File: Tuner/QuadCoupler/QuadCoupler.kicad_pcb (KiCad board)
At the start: 2 copper layers, 100 x 100 mm, 78 parts, among them J1 Conn_01x02, J10 Conn_01x02, J2 Conn_Coaxial, J21 Conn_01x01, J22 Conn_01x01, J23 Conn_01x01, J24 Conn_01x01, J3 Conn_Coaxial, J4 Conn_Coaxial, J5 Conn_Coaxial, J6 Conn_Coaxial, J7 Conn_01x02, J8 Conn_01x02, J9 Conn_01x02

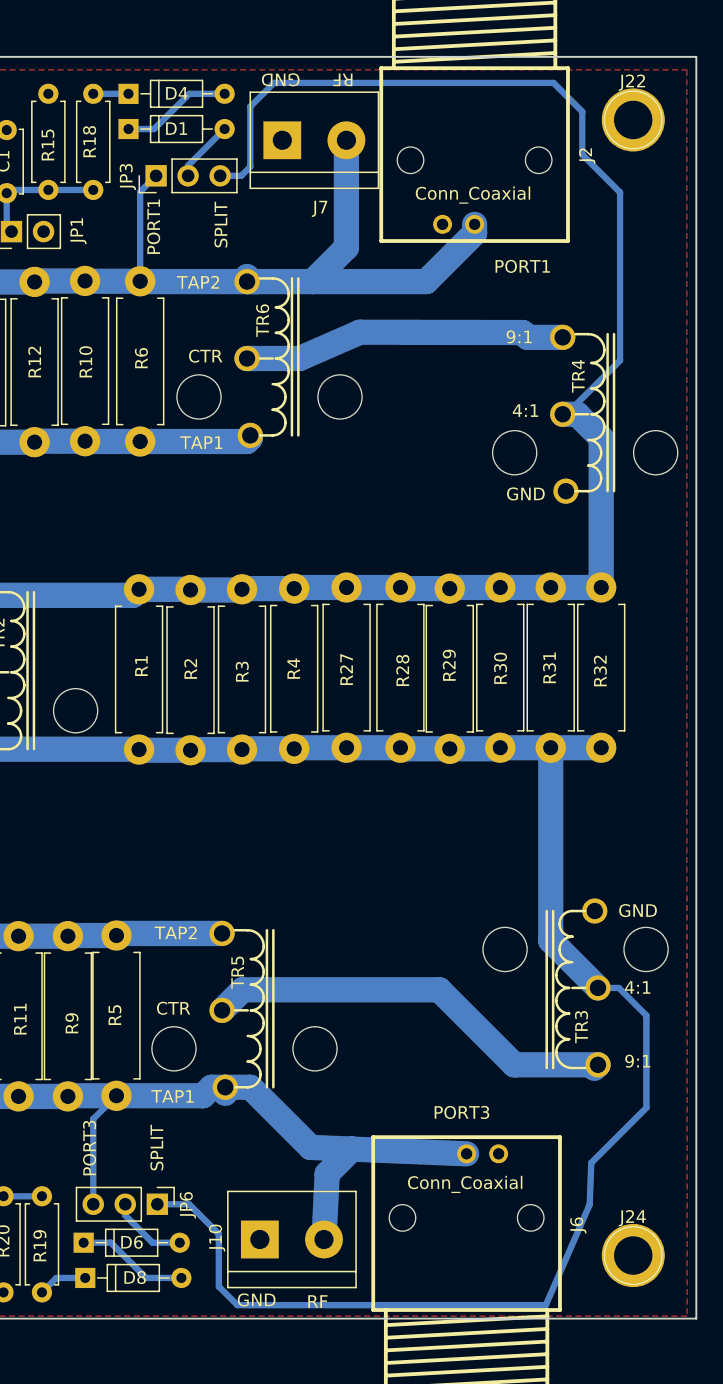
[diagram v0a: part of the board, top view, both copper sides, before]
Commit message: Changed DelayLine to short out sections
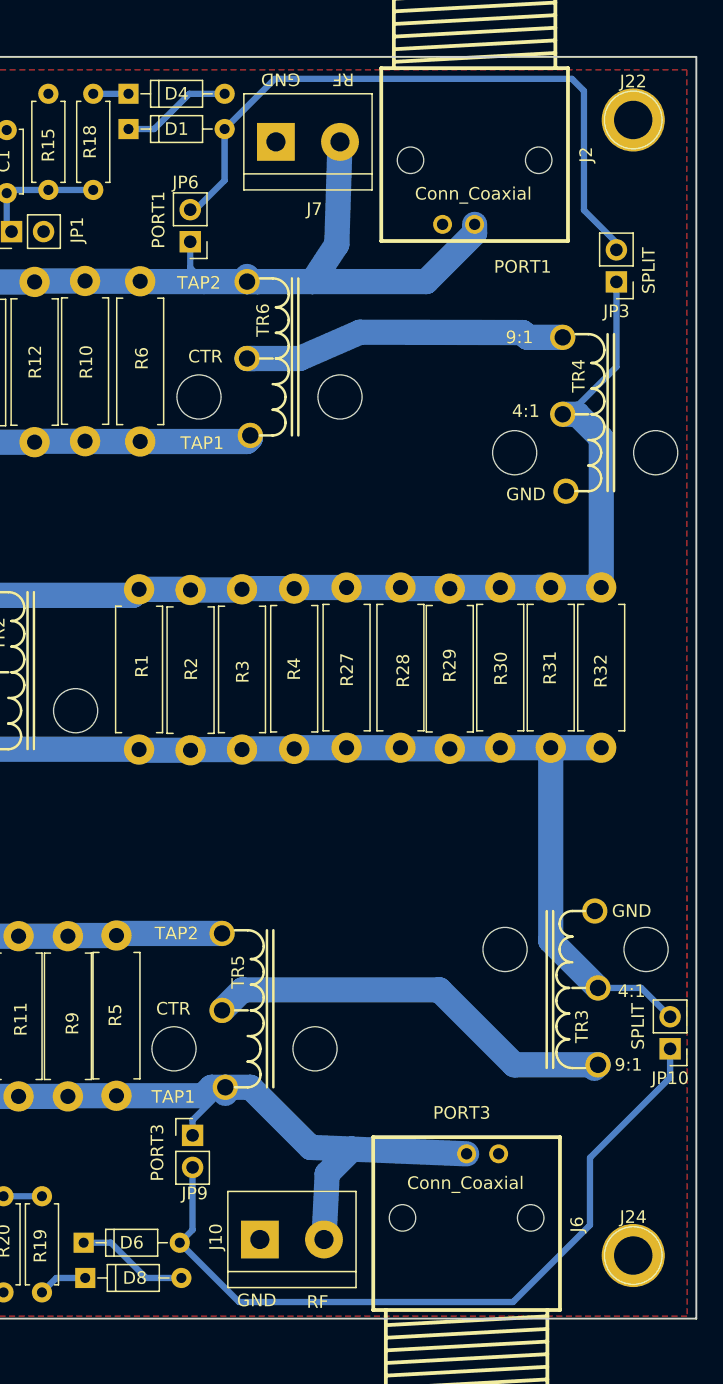
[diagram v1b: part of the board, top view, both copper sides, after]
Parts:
- added JP10: Jumper_NC_Small, Pin_Headers:Pin_Header_Straight_1x02_Pitch2.54mm, F.Cu at (137.9, 118.6)
- added JP9: Jumper_NC_Small, Pin_Headers:Pin_Header_Straight_1x02_Pitch2.54mm, F.Cu at (100.1, 125.5)
- JP3, JP6: value Jumper_NC_Dual -> Jumper_NC_Small; footprint Pin_Headers:Pin_Header_Straight_1x03_Pitch2.54mm -> Pin_Headers:Pin_Header_Straight_1x02_Pitch2.54mm
- moved JP6 76.3 mm to (99.9, 54.7), turned to 180 degrees
- moved JP3 37.4 mm to (133.7, 57.8), turned to 180 degrees
- moved J7 0.52 mm to (106.7, 46.7)
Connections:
- JP3 pad 1: Net-(J2-Pad1) -> Net-(JP3-Pad1)
- JP6 pad 1: Net-(JP6-Pad1) -> Net-(J2-Pad1)
- JP6 pad 2: Net-(D6-Pad2) -> Net-(D1-Pad2)
- R1 pad 1: Net-(JP3-Pad3) -> Net-(JP3-Pad1)
- R1 pad 2: Net-(JP6-Pad1) -> Net-(JP10-Pad2)
- R2 pad 1: Net-(JP3-Pad3) -> Net-(JP3-Pad1)
- R2 pad 2: Net-(JP6-Pad1) -> Net-(JP10-Pad2)
- R27 pad 1: Net-(JP3-Pad3) -> Net-(JP3-Pad1)
- R27 pad 2: Net-(JP6-Pad1) -> Net-(JP10-Pad2)
- R28 pad 1: Net-(JP3-Pad3) -> Net-(JP3-Pad1)
- R28 pad 2: Net-(JP6-Pad1) -> Net-(JP10-Pad2)
- R29 pad 1: Net-(JP3-Pad3) -> Net-(JP3-Pad1)
- R29 pad 2: Net-(JP6-Pad1) -> Net-(JP10-Pad2)
- R3 pad 1: Net-(JP3-Pad3) -> Net-(JP3-Pad1)
- R3 pad 2: Net-(JP6-Pad1) -> Net-(JP10-Pad2)
- R30 pad 1: Net-(JP3-Pad3) -> Net-(JP3-Pad1)
- R30 pad 2: Net-(JP6-Pad1) -> Net-(JP10-Pad2)
- R31 pad 1: Net-(JP3-Pad3) -> Net-(JP3-Pad1)
- R31 pad 2: Net-(JP6-Pad1) -> Net-(JP10-Pad2)
- R32 pad 1: Net-(JP3-Pad3) -> Net-(JP3-Pad1)
- R32 pad 2: Net-(JP6-Pad1) -> Net-(JP10-Pad2)
- R4 pad 1: Net-(JP3-Pad3) -> Net-(JP3-Pad1)
- R4 pad 2: Net-(JP6-Pad1) -> Net-(JP10-Pad2)
- TR2 pad 1: Net-(JP6-Pad1) -> Net-(JP10-Pad2)
- TR2 pad 3: Net-(JP3-Pad3) -> Net-(JP3-Pad1)
- TR3 pad 2: Net-(JP6-Pad1) -> Net-(JP10-Pad2)
- TR4 pad 2: Net-(JP3-Pad3) -> Net-(JP3-Pad1)
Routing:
- net Net-(JP6-Pad1): track 136.9 -> 0.00 mm
- net Net-(JP3-Pad3): track 130.9 -> 0.00 mm
- net Net-(JP3-Pad1): track 0.00 -> 80.9 mm
- net Net-(JP10-Pad2): track 0.00 -> 76.8 mm
- net Net-(D6-Pad2): track 6.10 -> 60.0 mm
- net Net-(D1-Pad2): track 4.91 -> 51.9 mm
- net Net-(J2-Pad1): track 88.5 -> 82.5 mm
- net Net-(J10-Pad2): track 84.5 -> 80.0 mm

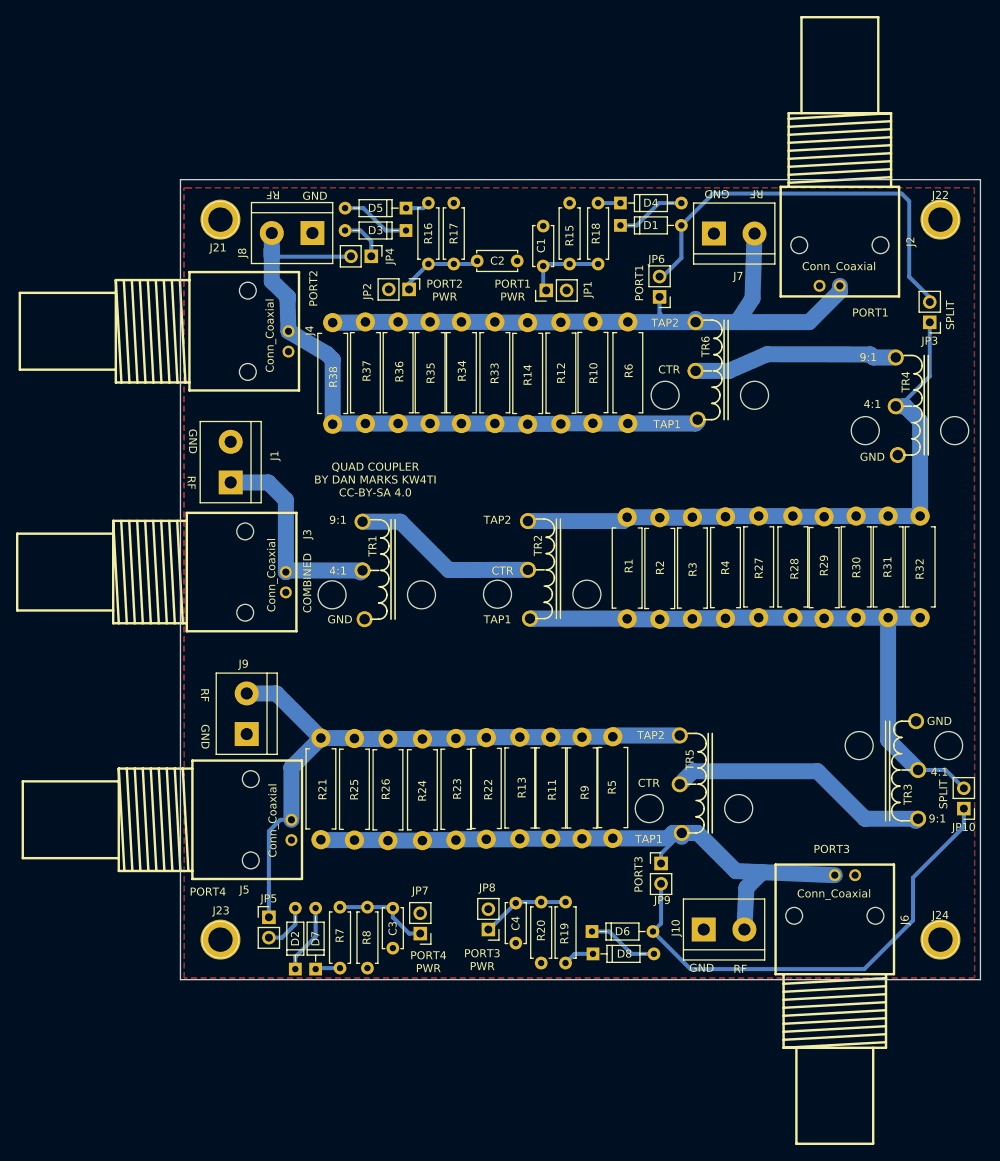
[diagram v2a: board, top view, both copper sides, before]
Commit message: Added more instrumentation to TandemMatch, fixed grounding issue
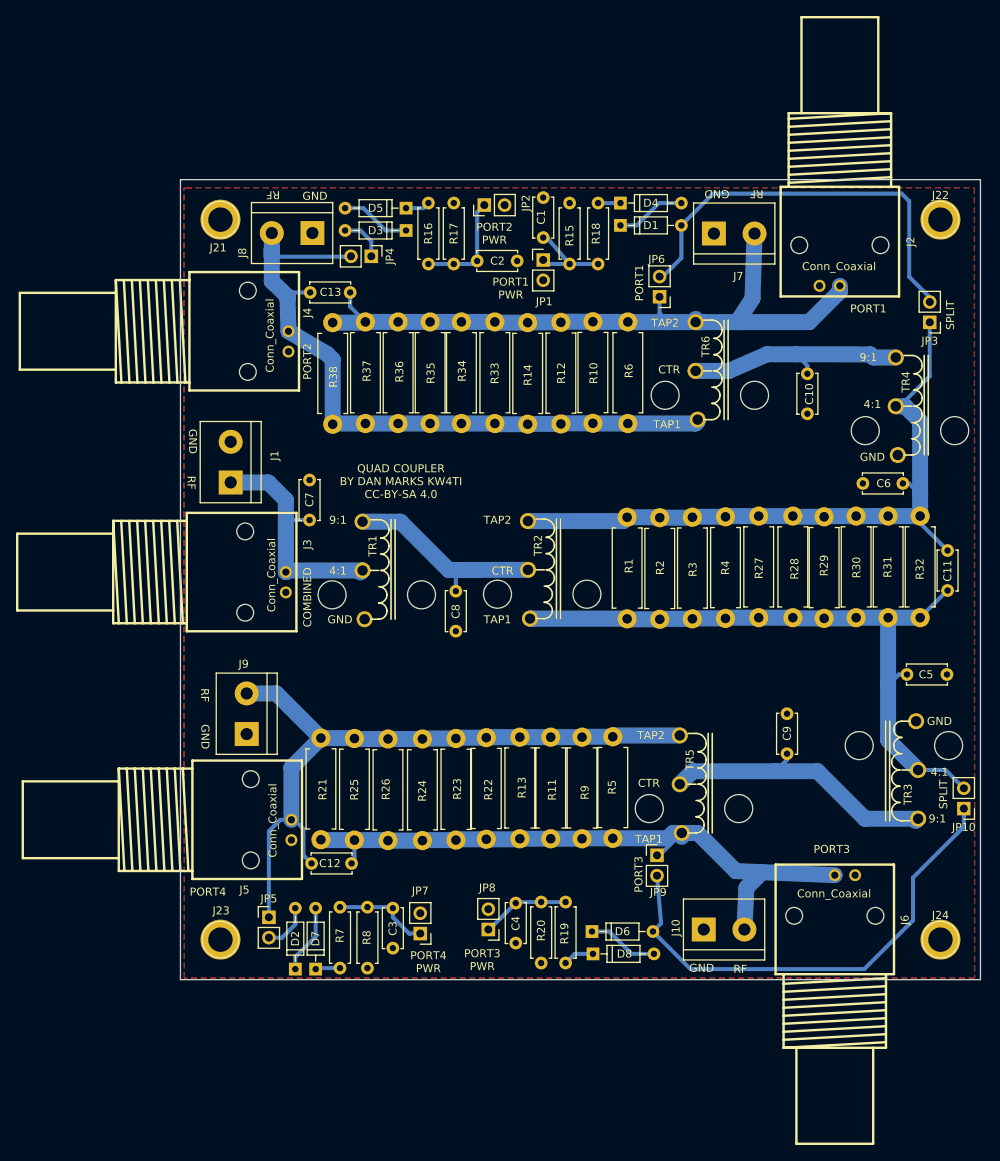
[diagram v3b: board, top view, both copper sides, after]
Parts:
- added C10: NC, Capacitors_THT:C_Disc_D5.0mm_W2.5mm_P5.00mm, F.Cu at (118.4, 64.3)
- added C11: NC, Capacitors_THT:C_Disc_D5.0mm_W2.5mm_P5.00mm, F.Cu at (135.9, 86.4)
- added C12: NC, Capacitors_THT:C_Disc_D5.0mm_W2.5mm_P5.00mm, F.Cu at (56.4, 125.5)
- added C13: NC, Capacitors_THT:C_Disc_D5.0mm_W2.5mm_P5.00mm, F.Cu at (61.2, 54.1)
- added C5: NC, Capacitors_THT:C_Disc_D5.0mm_W2.5mm_P5.00mm, F.Cu at (130.8, 101.9)
- added C6: NC, Capacitors_THT:C_Disc_D5.0mm_W2.5mm_P5.00mm, F.Cu at (130.3, 78.0)
- added C7: NC, Capacitors_THT:C_Disc_D5.0mm_W2.5mm_P5.00mm, F.Cu at (56.1, 82.5)
- added C8: NC, Capacitors_THT:C_Disc_D5.0mm_W2.5mm_P5.00mm, F.Cu at (74.4, 91.4)
- added C9: NC, Capacitors_THT:C_Disc_D5.0mm_W2.5mm_P5.00mm, F.Cu at (115.8, 111.8)
- moved JP2 14.1 mm to (78.0, 43.2), turned to 90 degrees
- moved JP1 3.83 mm to (85.3, 50.0), turned to 0 degrees
- moved C1 3.56 mm to (85.3, 47.2)
- moved JP9 1.14 mm to (99.6, 124.5)
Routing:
- net Net-(C11-Pad1): track 80.9 -> 89.4 mm
- net Net-(C11-Pad2): track 76.8 -> 84.5 mm
- net Net-(C12-Pad1): track 82.6 -> 89.4 mm
- net Net-(C13-Pad1): track 82.5 -> 87.0 mm
- net Net-(C7-Pad1): track 26.8 -> 30.6 mm
- net Net-(C2-Pad1): track 10.6 -> 13.8 mm
- net Net-(C10-Pad1): track 26.2 -> 29.2 mm
- net Net-(C8-Pad1): track 23.2 -> 26.2 mm
- net Net-(C13-Pad2): track 85.8 -> 88.8 mm
- net Net-(C9-Pad1): track 33.3 -> 36.1 mm
- net Net-(C12-Pad2): track 80.0 -> 82.4 mm
- net Net-(C1-Pad1): track 10.2 -> 12.1 mm
- net Net-(D6-Pad2): track 60.0 -> 61.0 mm
- net GND: track 0.00 -> 0.54 mm

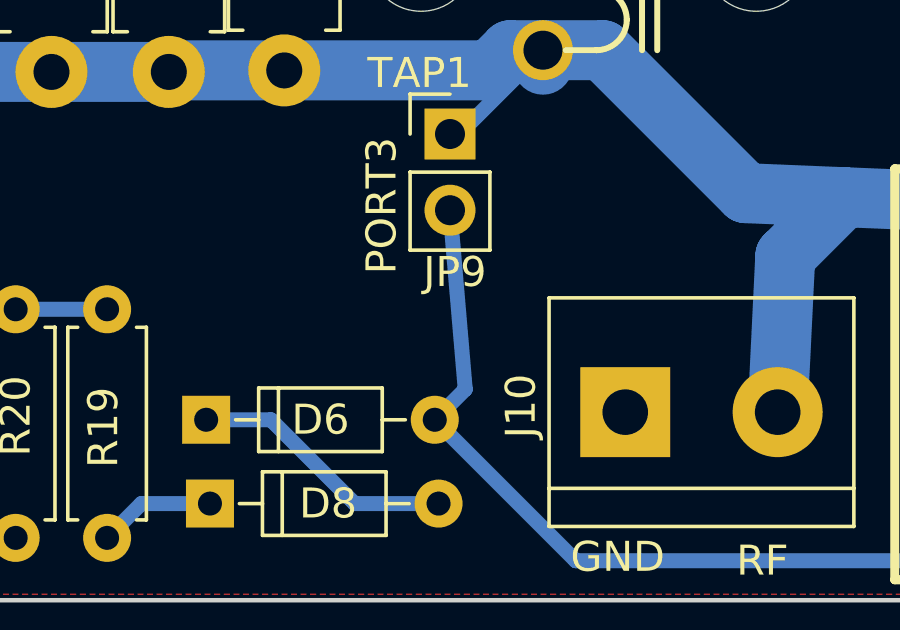
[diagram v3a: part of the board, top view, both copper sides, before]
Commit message: Removed 1k resistors, did some more rearranging on TandemMatch
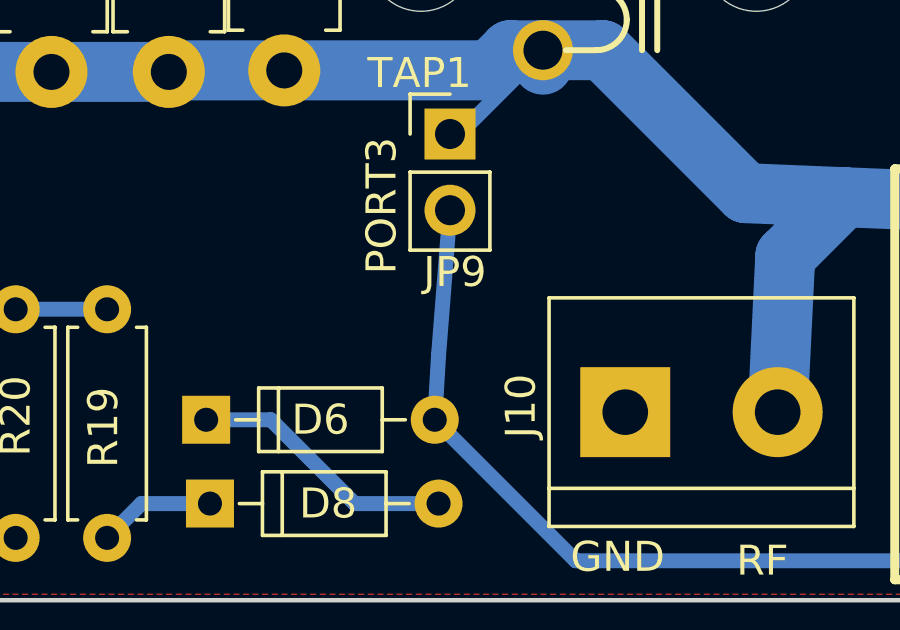
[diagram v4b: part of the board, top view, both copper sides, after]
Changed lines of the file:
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@@
   )
   (setup
-    (last_trace_width 0.5)
+    (last_trace_width 0.25)
     (user_trace_width 0.35)
     (user_trace_width 0.5)
@@
   (segment (start 131.572 127.254) (end 131.572 132.588) (width 0.5) (layer B.Cu) (net 9))
   (segment (start 137.922 120.904) (end 131.572 127.254) (width 0.5) (layer B.Cu) (net 9))
-  (segment (start 99.568 127) (end 100.076 132.969) (width 0.5) (layer B.Cu) (net 9) (status 10))
-  (segment (start 100.076 132.969) (end 99.06 133.985) (width 0.5) (layer B.Cu) (net 9))
+  (segment (start 99.568 127) (end 99.187 131.826) (width 0.5) (layer B.Cu) (net 9) (status 400010))
+  (segment (start 99.187 131.826) (end 99.06 133.985) (width 0.5) (layer B.Cu) (net 9) (status 800000))
   (segment (start 68.199 43.561) (end 70.358 43.561) (width 0.5) (layer B.Cu) (net 10))
   (segment (start 70.358 43.561) (end 70.993 42.926) (width 0.5) (layer B.Cu) (net 10))
@@
   (segment (start 129.413 68.326) (end 129.6924 68.326) (width 0.5) (layer B.Cu) (net 19))
   (segment (start 129.413 68.326) (end 130.302 68.326) (width 0.5) (layer B.Cu) (net 19))
-  (segment (start 56.134 82.55) (end 53.1724 82.55) (width 0.5) (layer B.Cu) (net 20) (status 400000))
+  (segment (start 56.134 82.55) (end 53.1724 82.55) (width 0.5) (layer B.Cu) (net 20))
   (segment (start 53.1724 82.55) (end 53.34 82.55) (width 0.5) (layer B.Cu) (net 20))
   (segment (start 53.34 82.55) (end 53.1724 82.55) (width 0.5) (layer B.Cu) (net 20))
